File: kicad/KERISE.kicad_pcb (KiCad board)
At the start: 2 copper layers, 46.5 x 50 mm, 145 parts, among them J1 COM, P1 ANT, P10 Partition, P11 PR_Host, P12 PR_Slave, P13 Partition, P14 Partition, P15 Partition, P16 Partition, P17 Fan, P18 ENC_Host, P19 ENC_Slave, P2 Motor_L, P20 ToF_Host, P21 ToF_Slave, P22 ENC_Host, P23 ENC_Slave, P24 PR_Host, P25 PR_Slave, P26 Partition, P27 Partition, P28 Partition, P29 Partition, P3 Motor_R, P30 PR_Host, P31 PR_Slave, P32 Partition, P33 Partition, P34 Partition, P35 Partition, P4 Battery, P5 PR_Host, P6 PR_Slave, P7 Partition, P8 Partition, P9 Partition, Q1 DMN3065LW-7, Q2 DMN3065LW-7, Q3 NX3020NAKW, Q4 DMN3065LW-7, Q5 DMN3065LW-7, Q6 DMN3065LW-7, SW1 SW_Push, SW2 SW_Push, U1 FLASH, U10 AS5048A, U11 ICM-20602, U12 AD8601, U13 AD8601, U2 ESP32, U3 XTAL, U4 DRV8835, U5 LXDC2URxx, U6 AD8601, U7 AD8601, U8 AS5048A, U9 VL53L0X

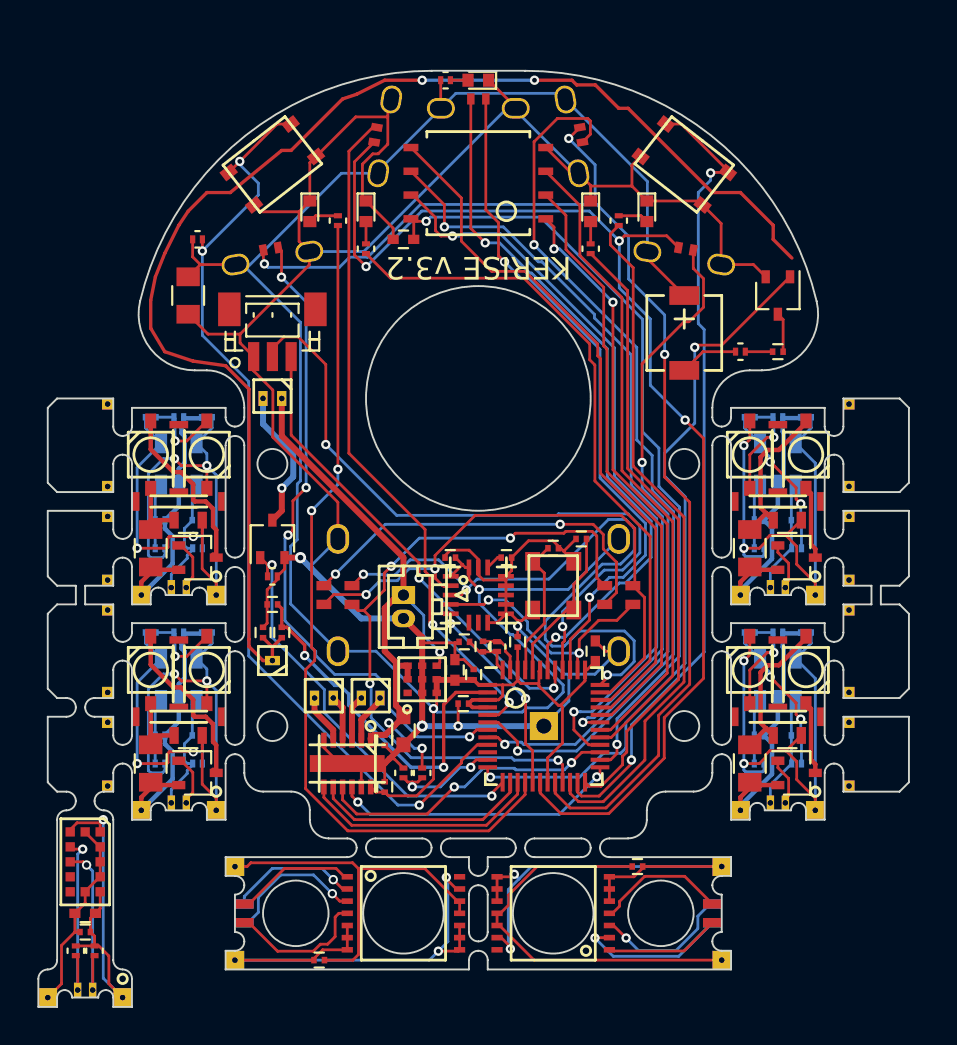
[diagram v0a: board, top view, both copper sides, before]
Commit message: フットプリントのミスを修正
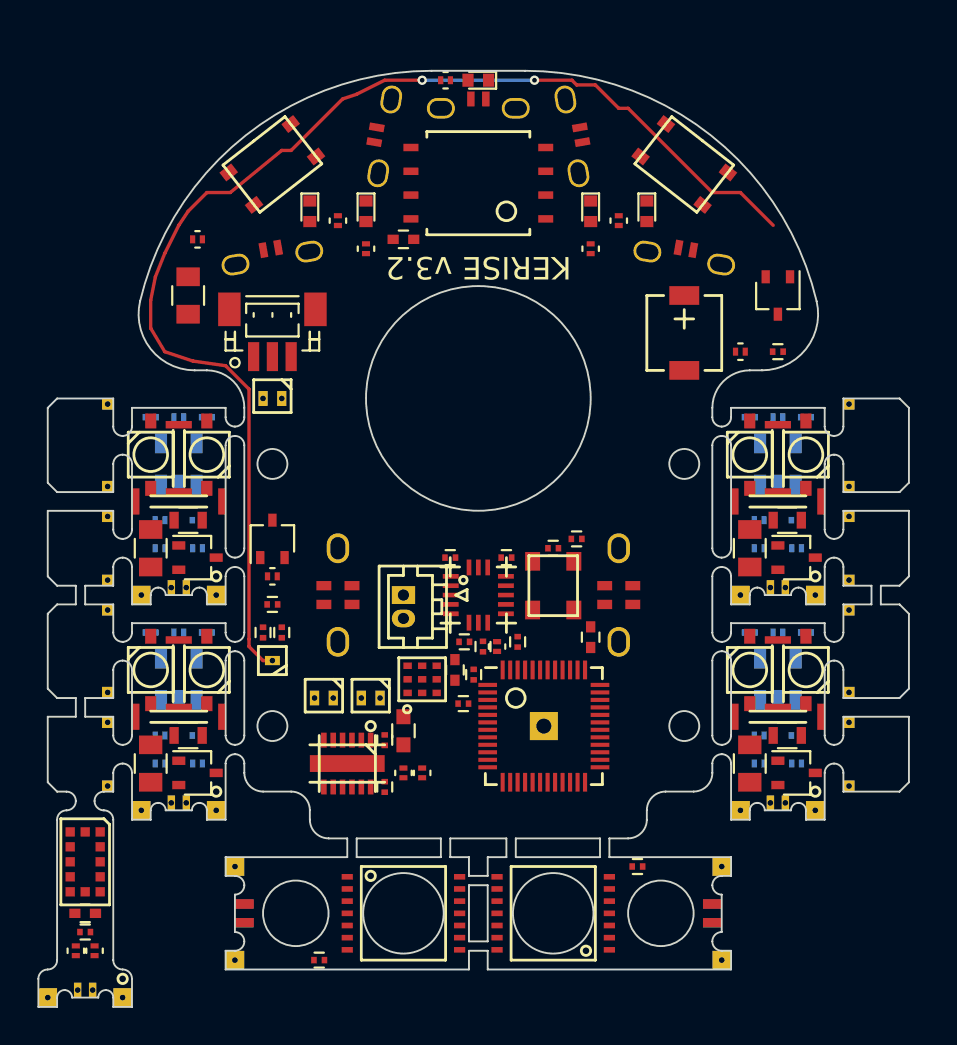
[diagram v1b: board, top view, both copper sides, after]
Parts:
- moved C6 0.79 mm to (154.5, 115.2)
- moved C11 0.25 mm to (153.8, 110.0)
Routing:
- net GND: track 155.0 -> 0.00 mm, vias 4 -> 0
- net +3V3: track 127.3 -> 0.00 mm, vias 2 -> 0
- net PR-LED-SL: track 65.5 -> 0.00 mm, vias 3 -> 0
- net PR-LED-SR: track 64.7 -> 0.00 mm, vias 3 -> 0
- net Net-(R2-Pad1): track 51.6 -> 0.00 mm, vias 3 -> 0
- net PR-RCV-SR: track 48.3 -> 0.00 mm, vias 2 -> 0
- net LED_4: track 45.1 -> 0.00 mm, vias 2 -> 0
- net BUTTON: track 43.1 -> 0.00 mm, vias 2 -> 0
- net VDD_SDIO: track 42.2 -> 0.00 mm, vias 2 -> 0
- net SHD/SD2: track 40.2 -> 0.00 mm, vias 2 -> 0
- net SCK/CLK: track 39.8 -> 0.00 mm, vias 2 -> 0
- net SPEAKER: track 39.0 -> 0.00 mm, vias 2 -> 0
- net SDI/SD1: track 37.9 -> 0.00 mm
- net I2C-SDA: track 37.8 -> 0.00 mm, vias 2 -> 0
- net UART-RX: track 37.1 -> 0.00 mm, vias 2 -> 0
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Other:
- outline, holes or cut-outs redrawn

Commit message: フットプリントを改良，アナログ電源を分離
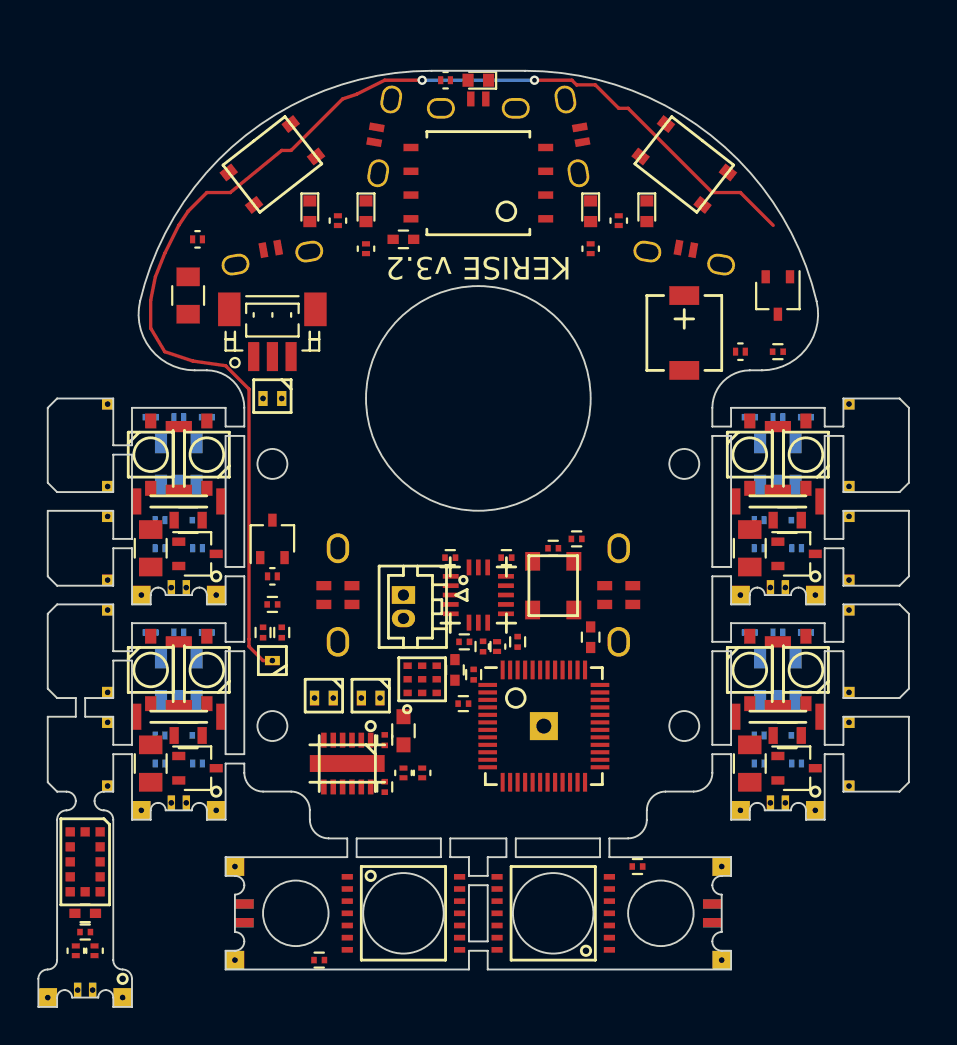
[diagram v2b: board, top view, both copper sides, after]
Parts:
- moved Q2 0.25 mm to (133.5, 122.2)
- moved Q5 0.25 mm to (165.5, 122.2)
- moved Q1 0.20 mm to (133.5, 110.8)
- moved Q6 0.20 mm to (165.5, 110.8)
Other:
- outline, holes or cut-outs redrawn

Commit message: 回路とフットプリントを改良
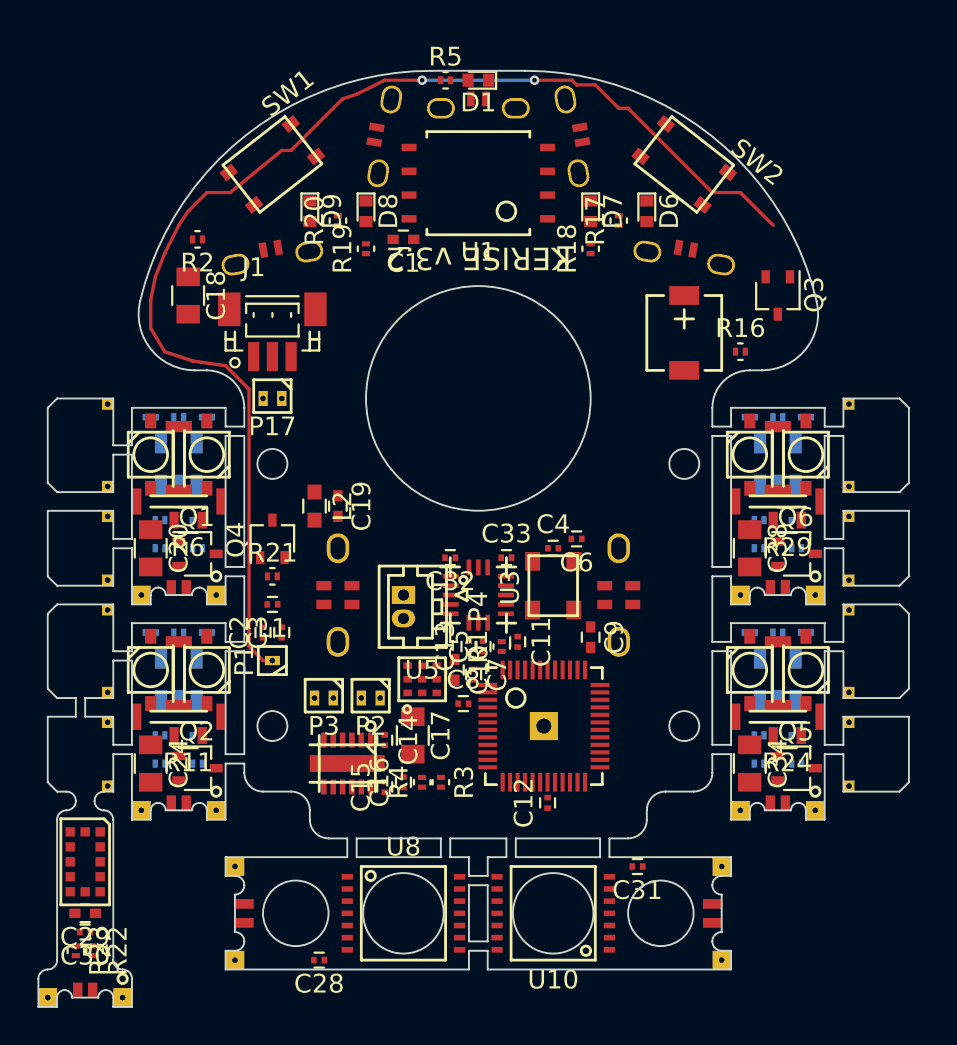
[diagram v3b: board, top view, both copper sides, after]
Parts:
- removed the C15 at (144.5, 120.2)
- removed the C25 at (164.5, 100.0)
- removed G***: LOGO, mouse:KERI_9mm
- added C12: 0.1u, Capacitors_SMD:C_0201, F.Cu at (152.2, 124.1)
- added C16: 0.1u, Capacitors_SMD:C_0201, F.Cu at (144.5, 123.0)
- added C17: 47u, Capacitors_SMD:C_0805, F.Cu at (145.0, 120.5)
- added C19: 10u, Capacitors_SMD:C_0402, F.Cu at (141.0, 108.2)
- added L2: 100u, Capacitors_SMD:C_0603, F.Cu at (139.8, 108.2)
- R16: value 1k -> 47
- moved R3 1.12 mm to (146.5, 123.0)
- moved R4 1.12 mm to (145.5, 123.0)
- moved C13 0.35 mm to (148.0, 115.8), turned to 90 degrees
- moved R1 0.25 mm to (149.8, 115.8)
- turned C31 to 180 degrees
- renumbered C7 to C10, C8 to C11, C12 to C13, C13 to C14, C14 to C15, C16 to C18, C17 to C20, C18 to C21, C19 to C22, C20 to C23, C21 to C24, C22 to C25, C23 to C26, C24 to C27, C26 to C28, C27 to C29, C28 to C30, C29 to C31, C30 to C32, C31 to C33, C32 to C34, C33 to C35, C34 to C36, C35 to C37, C36 to C38, C37 to C39, C9 to C4, C38 to C40, C39 to C41, C10 to C5, C11 to C6, C4 to C7, C5 to C8, C6 to C9
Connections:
- C11 pad 2: +3V3 -> VDDA
- C7 pad 2: +3V3 -> VDDA
- P11 pad 1: +3V3 -> VDDA
- P24 pad 1: +3V3 -> VDDA
- P30 pad 1: +3V3 -> VDDA
- P5 pad 1: +3V3 -> VDDA
- Q3 pad 3: Net-(C25-Pad2) (its old number) -> Net-(Q3-Pad3)
- R16 pad 2: Net-(C25-Pad1) (its old number) -> Net-(Q3-Pad3)
- U2 pad 1: +3V3 -> VDDA
- U2 pad 43: +3V3 -> VDDA
- U2 pad 46: +3V3 -> VDDA

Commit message: 自動配線1残し
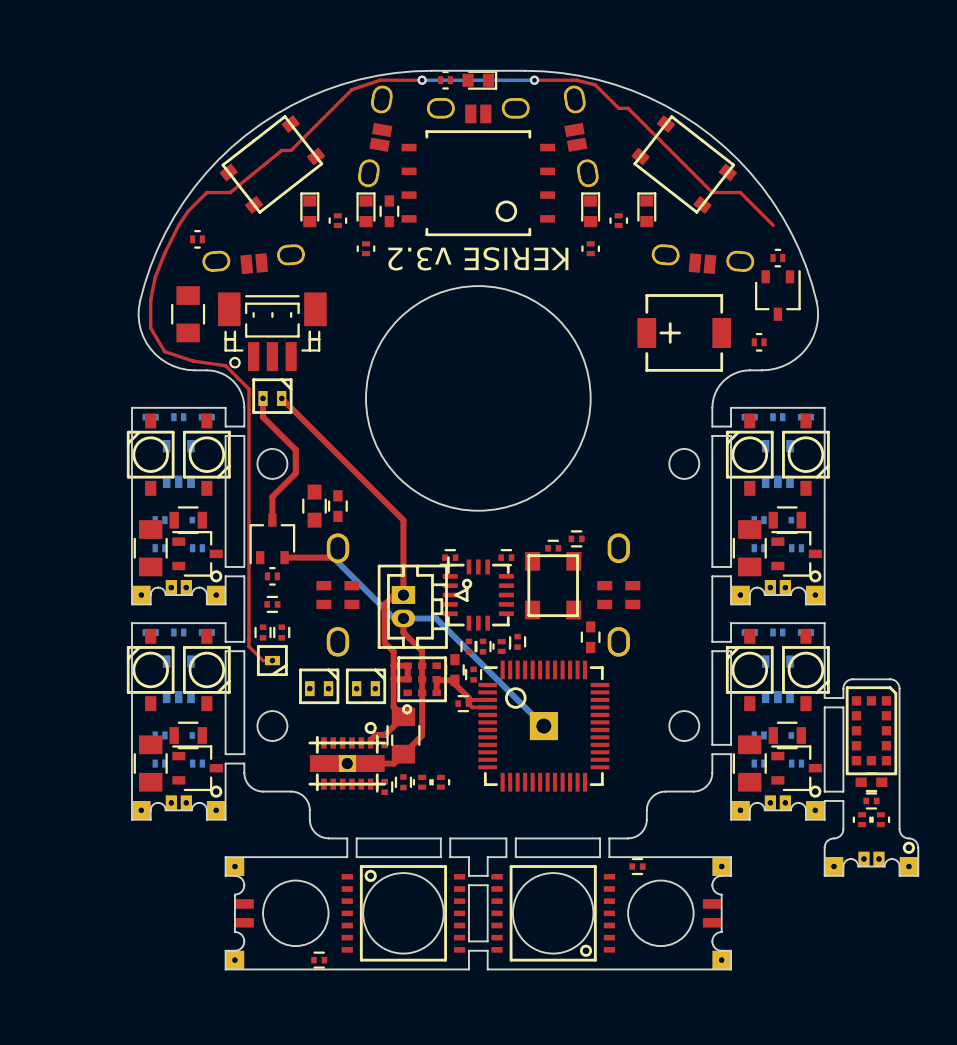
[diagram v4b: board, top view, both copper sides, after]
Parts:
- removed the C12 at (152.2, 124.1)
- removed the P10 at (129.0, 105.0)
- removed the P13 at (132.5, 117.2)
- removed the P14 at (168.0, 121.5)
- removed the P15 at (132.5, 119.5)
- removed the P16 at (168.0, 116.0)
- removed P26, P32: Partition, mouse:Partition_Host
- removed P27, P33: Partition, mouse:Partition_Slave
- removed P28, P34: Partition, mouse:Partition_Long_Host
- removed P29, P35: Partition, mouse:Partition_long_Slave
- removed the P7 at (132.5, 105.7)
- removed the P8 at (129.0, 110.5)
- removed the P9 at (132.5, 108.0)
- added R16: 10k, Resistors_SMD:R_0201, F.Cu at (164.5, 95.0)
- U12, U13, U6, U7: value AD8601 -> TLV316IDCKR; footprint TO_SOT_Packages_SMD:SOT-23-5 -> TO_SOT_Packages_SMD:SOT-353_SC-70-5
- moved C28 42.6 mm to (169.5, 123.0)
- moved C29 42.6 mm to (169.5, 124.0)
- moved P13 42.6 mm to (169.5, 127.5)
- moved R23 42.6 mm to (170.0, 125.0)
- moved R24 42.6 mm to (169.0, 125.0)
- moved U9 42.6 mm to (169.5, 120.2)
- moved C1 1.68 mm to (143.8, 92.5), turned to 90 degrees
- moved R17 1.12 mm to (163.5, 99.5)
- moved C17 1.00 mm to (133.0, 98.0)
- moved P16 1.00 mm to (136.5, 95.0), turned to 5 degrees
- moved P18 1.00 mm to (160.5, 95.0), turned to 355 degrees
- moved P2 0.56 mm to (142.5, 118.0)
- moved P3 0.56 mm to (140.0, 118.0)
- moved C16 0.50 mm to (144.5, 120.5)
- moved P5 0.50 mm to (143.0, 88.5)
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- renumbered C13 to C12, C14 to C13, C15 to C14, C16 to C15, C17 to C16, C18 to C17, C19 to C18, C20 to C19, C21 to C20, C22 to C21, C23 to C22, C24 to C23, C25 to C24, C26 to C25, C27 to C26, C28 to C27, C29 to C28, C30 to C29, C31 to C30, C32 to C31, C33 to C32, C34 to C33, C35 to C34, C36 to C35, C37 to C36, C38 to C37, C39 to C38, C40 to C39, C41 to C40, P18 to P10, P19 to P11, P20 to P12, P21 to P13, P22 to P14, P23 to P15, P24 to P16, P25 to P17, P30 to P18, P31 to P19, P11 to P7, P12 to P8, P17 to P9, R16 to R17, R17 to R18, R18 to R19, R19 to R20, R20 to R21, R21 to R22, R22 to R23, R23 to R24, R24 to R25, R25 to R26, R26 to R27, R27 to R28, R28 to R29, R29 to R30, R30 to R31, R31 to R32, R32 to R33, R33 to R34
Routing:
- net GND: track 0.00 -> 29.7 mm
- net +BATT: track 0.00 -> 26.3 mm
- net /Fan/fan_to_fet: track 0.00 -> 7.74 mm
- net +3V3: track 0.00 -> 5.48 mm
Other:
- board size 46.5 x 50 mm -> 42 x 48 mm

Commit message: 自動配線を適用，ロゴを追加
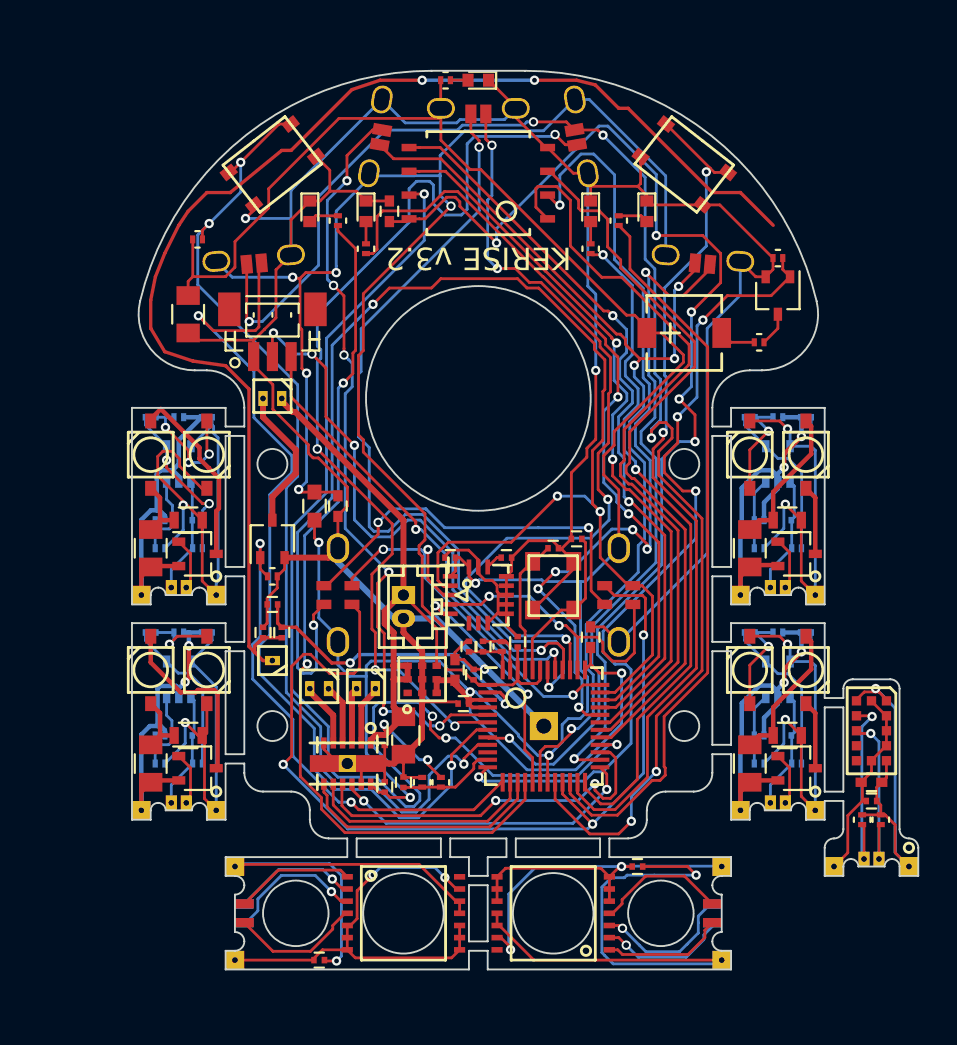
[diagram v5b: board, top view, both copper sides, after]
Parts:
- added G***: LOGO, mouse:KERI_9mm, B.Cu at (148.5, 116.0)
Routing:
- net GND: track 29.7 -> 191.7 mm, vias 0 -> 3
- net +3V3: track 5.48 -> 134.0 mm, vias 0 -> 6
- net VDDA: track 0.00 -> 89.4 mm, vias 0 -> 5
- net PR-LED-SR: track 0.00 -> 78.2 mm, vias 0 -> 6
- net SPI-SCLK: track 0.00 -> 74.9 mm, vias 0 -> 4
- net SHD/SD2: track 0.00 -> 64.0 mm, vias 0 -> 4
- net VDD_SDIO: track 0.00 -> 60.3 mm, vias 0 -> 6
- net Net-(R2-Pad1): track 0.00 -> 54.6 mm, vias 0 -> 3
- net PR-LED-SL: track 0.00 -> 53.0 mm, vias 0 -> 4
- net PR-RCV-SR: track 0.00 -> 51.9 mm, vias 0 -> 4
- net SPI-CS-ENC: track 0.00 -> 50.1 mm, vias 0 -> 3
- net PR-RCV-FL: track 0.00 -> 48.6 mm, vias 0 -> 2
- net LED_4: track 0.00 -> 46.4 mm, vias 0 -> 2
- net BUTTON: track 0.00 -> 45.7 mm, vias 0 -> 2
- net SDO/SD0: track 0.00 -> 44.2 mm, vias 0 -> 6
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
